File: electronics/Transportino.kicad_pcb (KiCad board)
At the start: 2 copper layers, 86.4 x 49.5 mm, 58 parts, among them J1 MOTOR_A_0, J2 MOTOR_A_1, J3 MOTOR_B_0, J4 MOTOR_B_1, J5 USB_B_Micro, SW1 PROG, SW2 SW_DPDT_x2, U1 RP2040, U2 TB6612FNG, U3 FLASH, U4 MPU-6050, U5 LM2575BU-ADJ, U6 NCP1117-3.3_SOT223, Y1 12Mhz

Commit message: Improved readme.md and added holes to mainboard
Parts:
- added H1: MountingHole, MountingHole:MountingHole_2.2mm_M2, F.Cu at (133.3, 68.6)
- added H2: MountingHole, MountingHole:MountingHole_2.2mm_M2, F.Cu at (207.2, 87.4)
- added H3: MountingHole, MountingHole:MountingHole_2.2mm_M2, F.Cu at (200.6, 70.9)
- added H4: MountingHole, MountingHole:MountingHole_2.2mm_M2, F.Cu at (128.3, 105.4)
- SW1: footprint Button_Switch_SMD:SW_Push_SPST_NO_Alps_SKRK -> Button_Switch_SMD:Button_SWITCH_6.1x3.7
- moved SW1 2.90 mm to (138.6, 86.5)
- moved ? 2.03 mm to (183.2, 80.3)
- turned R3 to 180 degrees
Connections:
- R3 pad 1: XOUT -> Net-(C18-Pad1)
- R3 pad 2: Net-(C18-Pad1) -> XOUT
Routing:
- net GND: track 461.4 -> 457.4 mm, vias 20 -> 19
- net XCL: track 55.5 -> 52.8 mm
- net SCL: track 32.6 -> 31.6 mm
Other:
- board text removed: "JLCJLCJLCJLC"

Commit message: Added link to the ArduCar repo
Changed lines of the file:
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@@
   (segment (start 155.448 82.804) (end 155.266489 82.985511) (width 0.18) (layer "F.Cu") (net 4))
   (segment (start 205.486 100.838) (end 205.486 102.313) (width 0.18) (layer "F.Cu") (net 4))
-  (segment (start 160.02 74.422) (end 153.924 74.422) (width 0.18) (layer "F.Cu") (net 4))
   (segment (start 155.448 82.804) (end 156.213258 83.569258) (width 0.18) (layer "F.Cu") (net 4))
   (segment (start 150.9485 93.98) (end 147.017 93.98) (width 0.18) (layer "F.Cu") (net 4))
@@
   (segment (start 155.583371 91.783786) (end 155.928696 91.438461) (width 0.18) (layer "F.Cu") (net 4))
   (segment (start 160.261227 91.31744) (end 159.879045 90.935258) (width 0.18) (layer "F.Cu") (net 4))
+  (segment (start 160.02 74.422) (end 154.686 74.422) (width 0.18) (layer "F.Cu") (net 4))
   (segment (start 155.497 81.026) (end 153.621 81.026) (width 0.18) (layer "F.Cu") (net 4))
   (segment (start 151.468202 89.238202) (end 153.037787 89.238202) (width 0.18) (layer "F.Cu") (net 4))
+  (segment (start 154.686 74.422) (end 153.924 75.184) (width 0.18) (layer "F.Cu") (net 4))
   (segment (start 153.924 71.78) (end 153.924 69.85) (width 0.18) (layer "F.Cu") (net 4))
   (segment (start 147.017 93.98) (end 145.747 92.71) (width 0.18) (layer "F.Cu") (net 4))
@@
   (segment (start 138.049 78.105) (end 137.922 78.232) (width 0.18) (layer "F.Cu") (net 4))
   (segment (start 153.924 85.09) (end 154.033787 85.09) (width 0.18) (layer "F.Cu") (net 4))
+  (segment (start 153.924 75.184) (end 153.924 78.08) (width 0.18) (layer "F.Cu") (net 4))
   (segment (start 128.79 94.476) (end 128.778 94.488) (width 0.18) (layer "F.Cu") (net 4))
   (segment (start 155.497 79.859) (end 155.6 79.756) (width 0.18) (layer "F.Cu") (net 4))
@@
   (segment (start 135.939 78.232) (end 137.922 78.232) (width 0.18) (layer "F.Cu") (net 4))
   (segment (start 161.48802 91.31744) (end 160.261227 91.31744) (width 0.18) (layer "F.Cu") (net 4))
+  (segment (start 153.924 74.422) (end 153.924 75.184) (width 0.18) (layer "F.Cu") (net 4))
   (segment (start 204.429 89.703) (end 204.47 89.662) (width 0.18) (layer "F.Cu") (net 4))
   (segment (start 132.759949 91.103949) (end 131.935949 91.103949) (width 0.18) (layer "F.Cu") (net 4))
@@
   (segment (start 156.714742 83.569258) (end 156.714742 82.243742) (width 0.18) (layer "F.Cu") (net 4))
   (segment (start 153.924 85.09) (end 154.599473 85.09) (width 0.18) (layer "F.Cu") (net 4))
-  (segment (start 153.924 74.422) (end 153.924 78.08) (width 0.18) (layer "F.Cu") (net 4))
   (segment (start 155.497 81.026) (end 155.497 79.859) (width 0.18) (layer "F.Cu") (net 4))
   (segment (start 133.858 80.313) (end 135.939 78.232) (width 0.18) (layer "F.Cu") (net 4))

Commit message: Added mechanics part and some renderings.
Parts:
- removed the ? at (183.2, 80.3)
- moved H3 0.13 mm to (200.7, 70.9)

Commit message: Added ros part
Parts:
- added 12V: TestPoint, TestPoint:TestPoint_Pad_D1.0mm, F.Cu at (199.7, 67.8)
- added 3V3: TestPoint, TestPoint:TestPoint_Pad_D1.0mm, F.Cu at (158.7, 78.8)
- added GND: TestPoint, TestPoint:TestPoint_Pad_D1.0mm, F.Cu at (135.9, 63.5)
- H1, H2, H3, H4: footprint MountingHole:MountingHole_2.2mm_M2 -> MountingHole:MountingHole_2.7mm_M2.5
- moved H3 0.98 mm to (201.4, 71.6)
- moved H2 0.48 mm to (206.9, 87.1)
- moved H4 0.31 mm to (128.0, 105.5)
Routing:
- net GND: track 457.4 -> 437.5 mm, vias 19 -> 18
- net +3V3: track 320.5 -> 325.5 mm
- net +12V: track 65.3 -> 67.9 mm

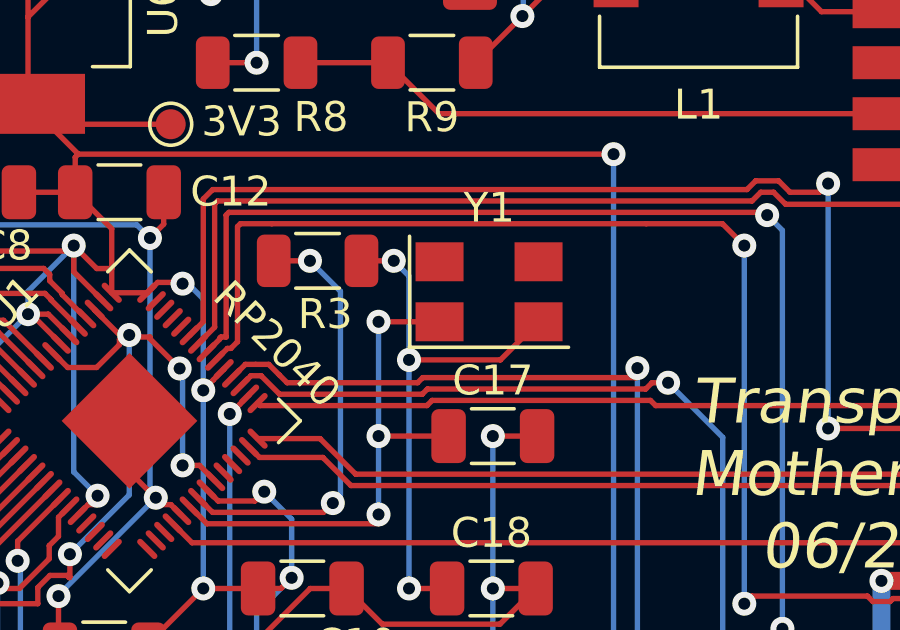
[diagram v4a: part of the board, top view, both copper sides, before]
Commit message: Changed wrong assigned crystal pin.
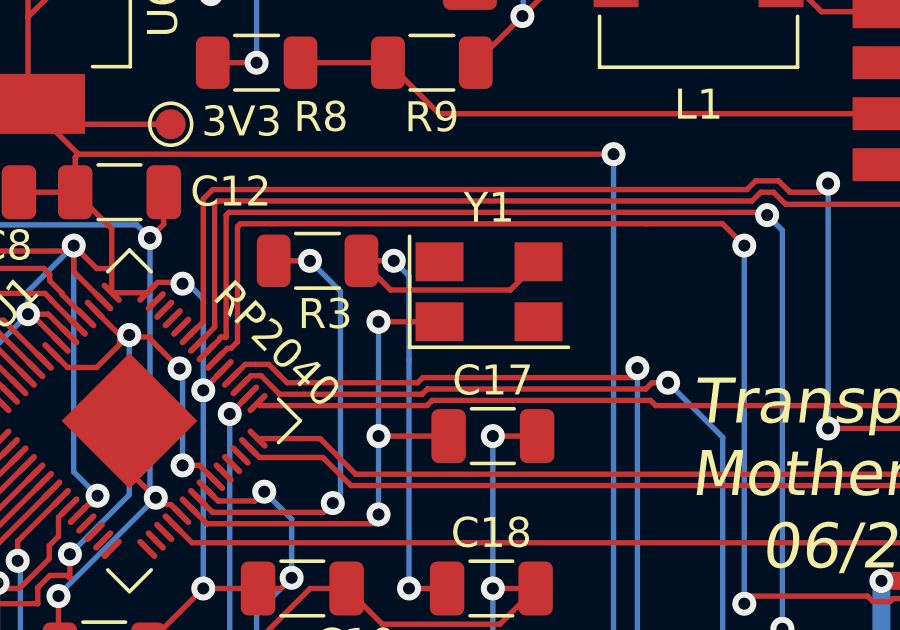
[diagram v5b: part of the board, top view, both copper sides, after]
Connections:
- Y1 pad 2: Net-(C18-Pad1) -> (no net)
- Y1 pad 3: (no net) -> Net-(C18-Pad1)
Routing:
- net Net-(C18-Pad1): track 18.3 -> 20.3 mm, vias 3 -> 2
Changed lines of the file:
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@@
       (net 6 "XIN") (pinfunction "1") (pintype "passive"))
     (pad "2" smd rect (at 1.65 1) (size 1.6 1.3) (layers "F.Cu" "F.Paste" "F.Mask")
-      (net 7 "Net-(C18-Pad1)") (pinfunction "2") (pintype "passive"))
-    (pad "3" smd rect (at 1.65 -1) (size 1.6 1.3) (layers "F.Cu" "F.Paste" "F.Mask"))
+      (pinfunction "2") (pintype "passive"))
+    (pad "3" smd rect (at 1.65 -1) (size 1.6 1.3) (layers "F.Cu" "F.Paste" "F.Mask")
+      (net 7 "Net-(C18-Pad1)"))
     (pad "4" smd rect (at -1.65 -1) (size 1.6 1.3) (layers "F.Cu" "F.Paste" "F.Mask"))
     (model "${KICAD6_3DMODEL_DIR}/Crystal.3dshapes/Crystal_SMD_5032-4Pin_5.0x3.2mm.wrl"
@@
   (segment (start 165.608 91.7665) (end 165.608 89.154) (width 0.18) (layer "B.Cu") (net 6))
   (segment (start 166.624 94.234) (end 167.894 94.234) (width 0.18) (layer "F.Cu") (net 7))
+  (segment (start 170.002 84.284) (end 166.0105 84.284) (width 0.18) (layer "F.Cu") (net 7))
   (segment (start 165.0385 83.312) (end 166.116 83.312) (width 0.18) (layer "F.Cu") (net 7))
-  (segment (start 169.672 86.614) (end 170.942 85.344) (width 0.18) (layer "F.Cu") (net 7))
-  (segment (start 166.624 86.614) (end 169.672 86.614) (width 0.18) (layer "F.Cu") (net 7))
+  (segment (start 170.792 83.344) (end 170.942 83.344) (width 0.18) (layer "F.Cu") (net 7))
+  (segment (start 166.0105 84.284) (end 165.0385 83.312) (width 0.18) (layer "F.Cu") (net 7))
+  (segment (start 170.942 83.344) (end 170.002 84.284) (width 0.18) (layer "F.Cu") (net 7))
   (via (at 166.624 94.234) (size 0.8) (drill 0.4) (layers "F.Cu" "B.Cu") (net 7))
   (via (at 166.116 83.312) (size 0.8) (drill 0.4) (layers "F.Cu" "B.Cu") (net 7))
-  (via (at 166.624 86.614) (size 0.8) (drill 0.4) (layers "F.Cu" "B.Cu") (net 7))
   (segment (start 166.624 86.614) (end 166.624 83.82) (width 0.18) (layer "B.Cu") (net 7))
   (segment (start 166.624 86.614) (end 166.624 94.234) (width 0.18) (layer "B.Cu") (net 7))

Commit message: Changed buzzer gpio pin.
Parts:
- J1: value MOTOR_A_0 -> MOTOR A0
- J2: value MOTOR_A_1 -> MOTOR A1
- J3: value MOTOR_B_0 -> MOTOR B0
- J4: value MOTOR_B_1 -> MOTOR B1
- TP2: renamed from 3V3; value TestPoint -> 3.3V
- TP3: renamed from 12V; value TestPoint -> 12V
- moved TP2 32.5 mm to (126.5, 74.0)
- moved TP3 14.8 mm to (185.0, 69.6)
- renumbered GND to TP1
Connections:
- U1 pad 11: unconnected-(U1-Pad11) -> BUZZ
- U1 pad 8: BUZZ -> unconnected-(U1-Pad8)
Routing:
- net +12V: track 67.9 -> 70.7 mm
- net STATUS_LED: track 21.1 -> 20.5 mm
- net BUZZ: track 18.3 -> 17.8 mm
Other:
- board text added: "Transportino Motherboard 07/2022"
- board text removed: "Transportino Motherboard 06/2022"
